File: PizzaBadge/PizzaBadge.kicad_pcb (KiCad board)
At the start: 2 copper layers, 95.2 x 95.2 mm, 169 parts, among them J1 BATTERY, J2 signal 1, J3 signal 1, J4 signal 1, J5 signal 1, J6 signal 1, J7 signal 1, J8 signal 1, J9 signal 1, Q1 NPN, Q2 NPN, Q3 NPN, Q4 NPN, Q5 NPN, Q6 NPN, Q7 NPN, Q8 NPN

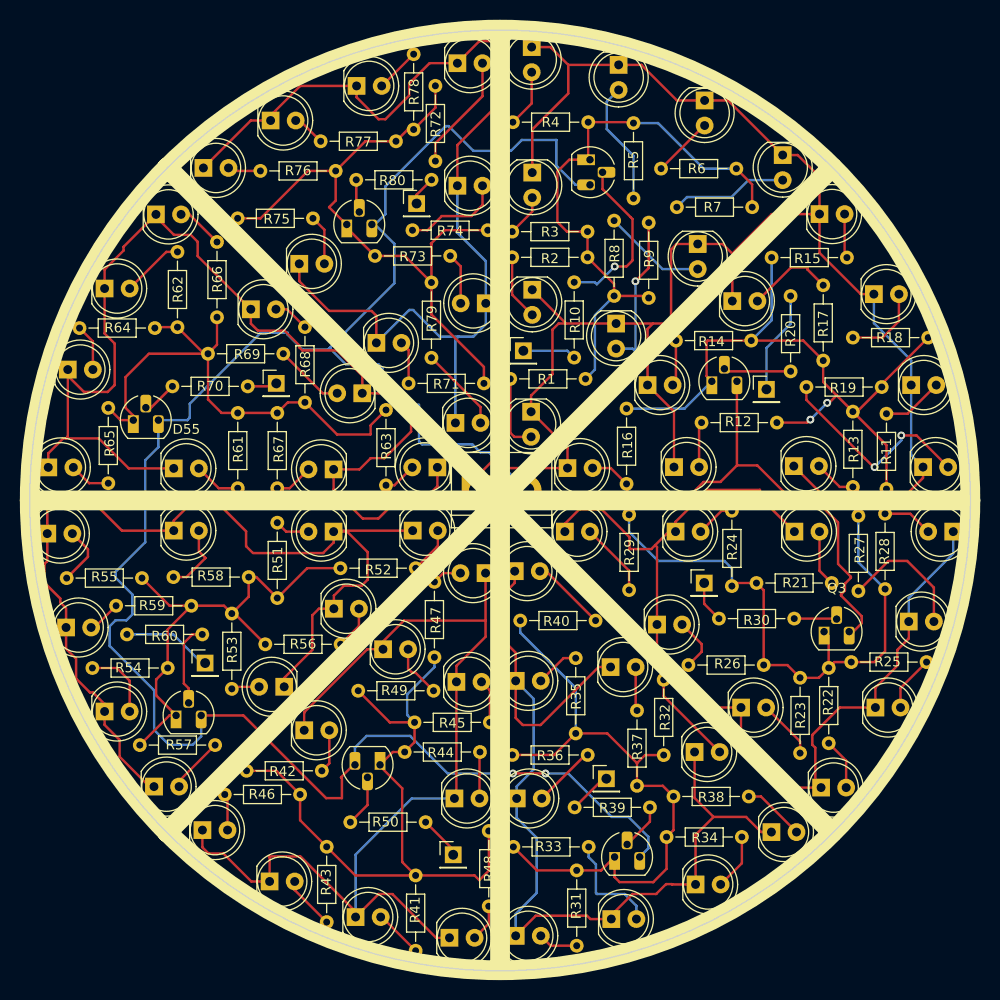
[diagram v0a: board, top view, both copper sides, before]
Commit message: fix scheme, fix board, add reset button, revision1
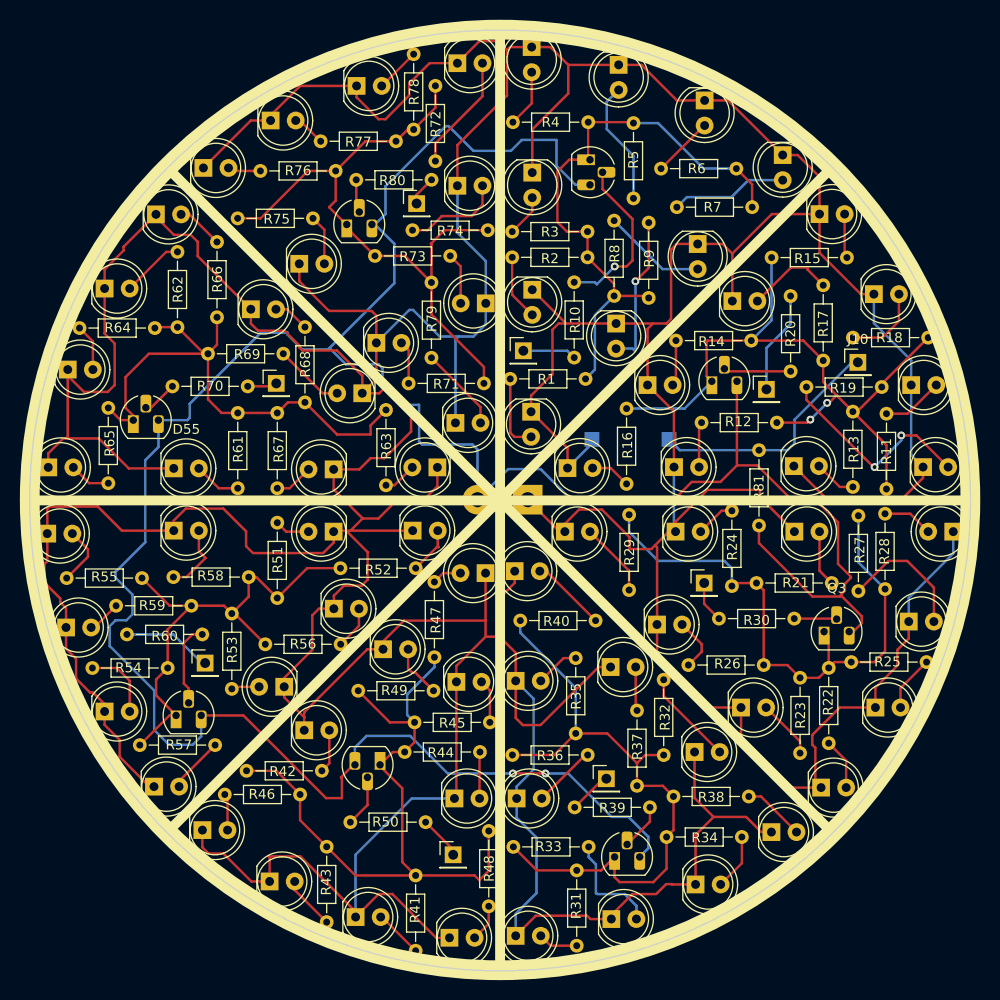
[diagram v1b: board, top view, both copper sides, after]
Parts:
- added J10: signal 1, Connector_PinHeader_2.54mm:PinHeader_1x01_P2.54mm_Vertical, F.Cu at (156.2, 71.3)
- added R81: 1K, Resistor_THT:R_Axial_DIN0204_L3.6mm_D1.6mm_P7.62mm_Horizontal, F.Cu at (146.2, 80.2)
- added SW1: RESET, Button_Switch_SMD:SW_SPST_CK_RS282G05A3, B.Cu at (133.2, 79.1)
- J1: moved to B.Cu
- R10, R20, R30, R39, R50, R60, R70, R80: value 4k7 -> 1K
- moved J1 5.27 mm to (122.8, 85.2), turned to 180 degrees
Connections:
- net 12V renamed 5V
- D19 pad 1: Net-(D19-Pad1) -> GND
- D20 pad 1: Net-(D19-Pad1) -> GND
- D21 pad 1: Net-(D19-Pad1) -> GND
- D22 pad 1: Net-(D19-Pad1) -> GND
- D23 pad 1: Net-(D19-Pad1) -> GND
- D24 pad 1: Net-(D19-Pad1) -> GND
- D25 pad 1: Net-(D19-Pad1) -> GND
- D26 pad 1: Net-(D19-Pad1) -> GND
- D27 pad 1: Net-(D19-Pad1) -> GND
- D28 pad 1: Net-(D28-Pad1) -> GND
- D29 pad 1: Net-(D28-Pad1) -> GND
- D30 pad 1: Net-(D28-Pad1) -> GND
- D31 pad 1: Net-(D28-Pad1) -> GND
- D32 pad 1: Net-(D28-Pad1) -> GND
- D33 pad 1: Net-(D28-Pad1) -> GND
- D34 pad 1: Net-(D28-Pad1) -> GND
- D35 pad 1: Net-(D28-Pad1) -> GND
- D36 pad 1: Net-(D28-Pad1) -> GND
- D37 pad 1: Net-(D37-Pad1) -> GND
- D38 pad 1: Net-(D37-Pad1) -> GND
- D39 pad 1: Net-(D37-Pad1) -> GND
- D40 pad 1: Net-(D37-Pad1) -> GND
- D41 pad 1: Net-(D37-Pad1) -> GND
- D42 pad 1: Net-(D37-Pad1) -> GND
- D43 pad 1: Net-(D37-Pad1) -> GND
- D44 pad 1: Net-(D37-Pad1) -> GND
- D45 pad 1: Net-(D37-Pad1) -> GND
- D46 pad 1: Net-(D46-Pad1) -> GND
- D47 pad 1: Net-(D46-Pad1) -> GND
- D48 pad 1: Net-(D46-Pad1) -> GND
- D49 pad 1: Net-(D46-Pad1) -> GND
- D50 pad 1: Net-(D46-Pad1) -> GND
- D51 pad 1: Net-(D46-Pad1) -> GND
- D52 pad 1: Net-(D46-Pad1) -> GND
- D53 pad 1: Net-(D46-Pad1) -> GND
- D54 pad 1: Net-(D46-Pad1) -> GND
- D55 pad 1: Net-(D55-Pad1) -> GND
- D56 pad 1: Net-(D55-Pad1) -> GND
- D57 pad 1: Net-(D55-Pad1) -> GND
- D58 pad 1: Net-(D55-Pad1) -> GND
- D59 pad 1: Net-(D55-Pad1) -> GND
- D60 pad 1: Net-(D55-Pad1) -> GND
- D61 pad 1: Net-(D55-Pad1) -> GND
- D62 pad 1: Net-(D55-Pad1) -> GND
- D63 pad 1: Net-(D55-Pad1) -> GND
- D64 pad 1: Net-(D64-Pad1) -> GND
- D65 pad 1: Net-(D64-Pad1) -> GND
- D66 pad 1: Net-(D64-Pad1) -> GND
- D67 pad 1: Net-(D64-Pad1) -> GND
- D68 pad 1: Net-(D64-Pad1) -> GND
- D69 pad 1: Net-(D64-Pad1) -> GND
- D70 pad 1: Net-(D64-Pad1) -> GND
- D71 pad 1: Net-(D64-Pad1) -> GND
- D72 pad 1: Net-(D64-Pad1) -> GND
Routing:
- net GND: track 188.4 -> 835.9 mm
- net Net-(D55-Pad1): track 115.2 -> 0.00 mm
- net Net-(D64-Pad1): track 108.6 -> 0.00 mm
- net Net-(D37-Pad1): track 103.7 -> 0.00 mm
- net Net-(D19-Pad1): track 101.5 -> 0.00 mm
- net Net-(D46-Pad1): track 100.6 -> 0.00 mm
- net Net-(D28-Pad1): track 99.9 -> 0.00 mm
- net RESET: track 0.00 -> 24.6 mm
- net 5V: track 264.0 -> 282.4 mm, vias 2 -> 3
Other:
- board text added: "5V"
- board text added: "GND"
- board text added: "Hold 5s for factory reset"
- board text added: "PizzaBadge rev1"
- board text added: "by bosko"

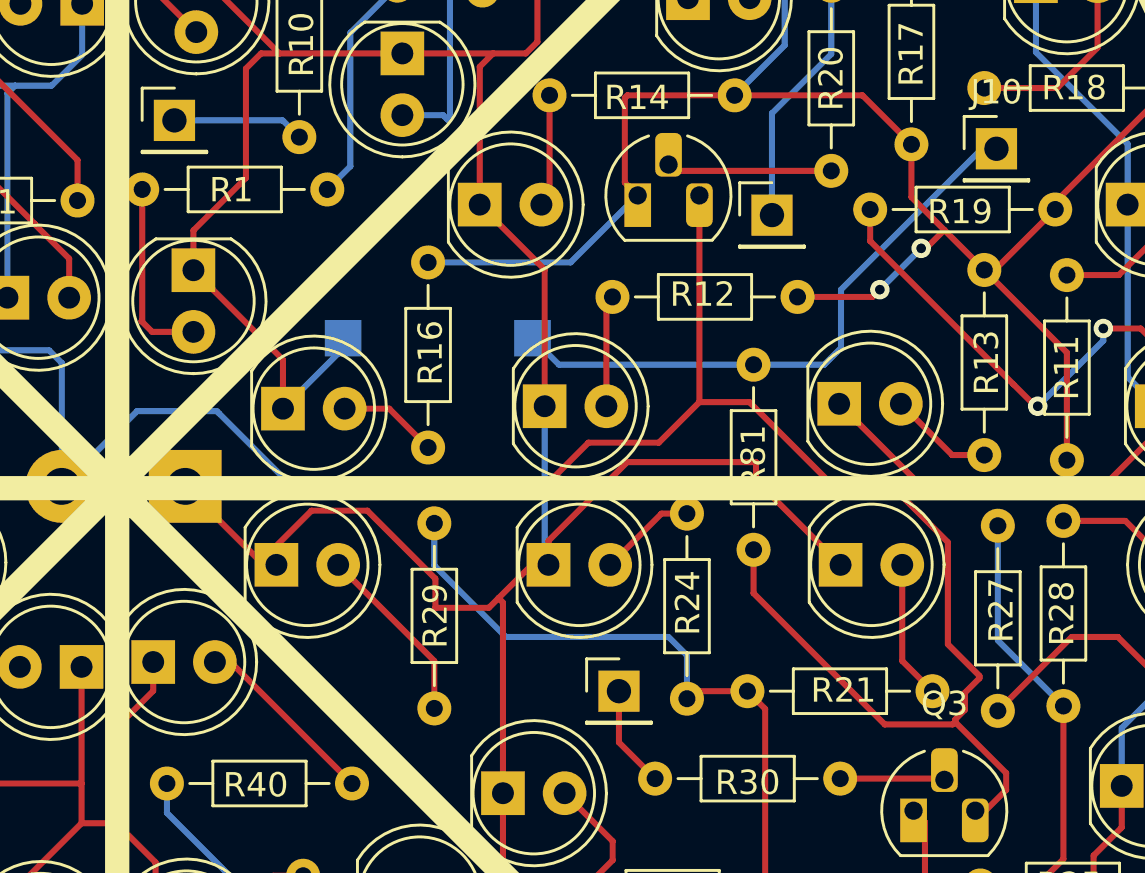
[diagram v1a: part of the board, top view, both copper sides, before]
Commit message: add reset button
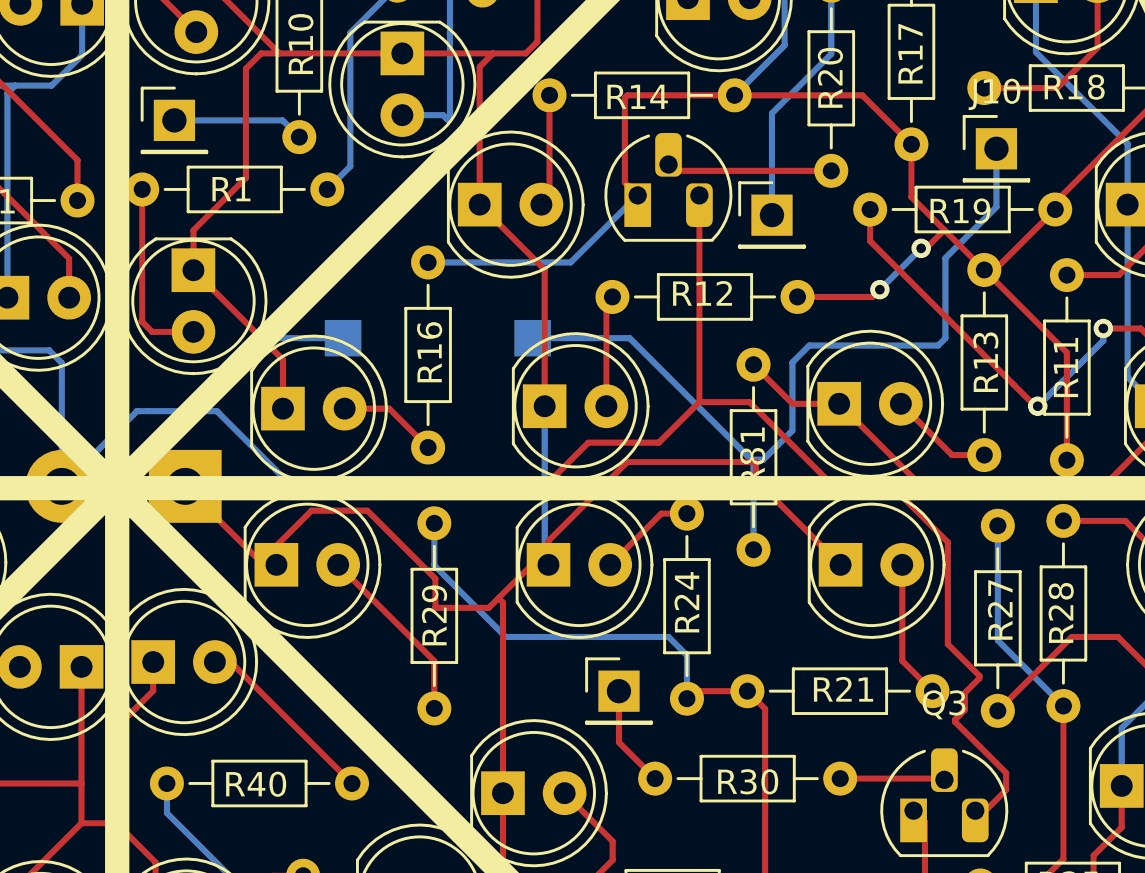
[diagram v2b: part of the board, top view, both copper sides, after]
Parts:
- R81: value 1K -> 10K
- turned SW1 to 180 degrees
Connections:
- R81 pad 1: RESET -> GND
- R81 pad 2: 5V -> RESET
- SW1 pad 1: GND -> RESET
- SW1 pad 2: RESET -> 5V
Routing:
- net RESET: track 24.6 -> 35.2 mm
- net 5V: track 282.4 -> 277.4 mm

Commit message: update
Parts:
- J10: value signal 1 -> PIN RESET
- J2: value signal 1 -> 1; moved to B.Cu
- J3: value signal 1 -> 2; moved to B.Cu
- J4: value signal 1 -> 3; moved to B.Cu
- J5: value signal 1 -> 4; moved to B.Cu
- J6: value signal 1 -> 5; moved to B.Cu
- J7: value signal 1 -> 6; moved to B.Cu
- J8: value signal 1 -> 7; moved to B.Cu
- J9: value signal 1 -> 8; moved to B.Cu
- R1, R11, R12, R13, R14, R15, R16, R17, R18, R19, R2, R21, R22, R23, R24, R25, R26, R27, R28, R29, R3, R31, R32, R33, R34, R35, R36, R37, R38, R4, R40, R41, R42, R43, R44, R45, R46, R47, R48, R49, R5, R51, R52, R53, R54, R55, R56, R57, R58, R59, R6, R61, R62, R63, R64, R65, R66, R67, R68, R69, R7, R71, R72, R73, R74, R75, R76, R77, R78, R79, R8, R9: value 200 -> 330
- R10, R20, R30, R39, R50, R60, R70, R80: value 1K -> 10K
- turned J2 to 180 degrees
- turned J3 to 180 degrees
- turned J4 to 180 degrees
- turned J5 to 180 degrees
- turned J6 to 180 degrees
- turned J7 to 180 degrees
- turned J8 to 180 degrees
- turned J9 to 180 degrees

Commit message: silk improve
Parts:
- RESET: renamed from J10; moved to B.Cu
- turned RESET to 180 degrees
- renumbered R39 to 10K, R70 to 10K, R30 to 10K, R60 to 10K, R80 to 10K, R20 to 10K, R50 to 10K, R10 to 10K, R63 to 330, R48 to 330, R9 to 330, R68 to 330, R7 to 330, R18 to 330, R2 to 330, R21 to 330, R34 to 330, R28 to 330, R49 to 330, R29 to 330, R79 to 330, R66 to 330, R23 to 330, R37 to 330, R42 to 330, R15 to 330, R40 to 330, R1 to 330, R32 to 330, R62 to 330, R5 to 330, R54 to 330, R19 to 330, R43 to 330, R71 to 330, R35 to 330, R81 to 330, R44 to 330, R74 to 330, R45 to 330, R53 to 330, R14 to 330, R16 to 330, R26 to 330, R13 to 330, R51 to 330, R25 to 330, R61 to 330, R56 to 330, R3 to 330, R17 to 330, R8 to 330, R22 to 330, R46 to 330, R47 to 330, R58 to 330, R38 to 330, R6 to 330, R11 to 330, R65 to 330, R59 to 330, R75 to 330, R36 to 330, R4 to 330, R57 to 330, R72 to 330, R33 to 330, R78 to 330, R12 to 330, R41 to 330, R76 to 330, R77 to 330, R27 to 330, R64 to 330, R52 to 330, R55 to 330, R24 to 330, R69 to 330, R73 to 330, R67 to 330, R31 to 330
